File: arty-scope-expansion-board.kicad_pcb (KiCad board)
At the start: 4 copper layers, 109 x 86 mm, 75 parts, among them J1 PMOD_A, J2 PMOD_B, J3 PMOD_C, J4 PMOD_D, J5 Conn_Coaxial, U1 AD9288, U2 74LS374, U3 74LS374, U4 AD8370AREZ-RL7, U5 AD8132ARZ, U6 AD8132ARZ, U7 MCP4822

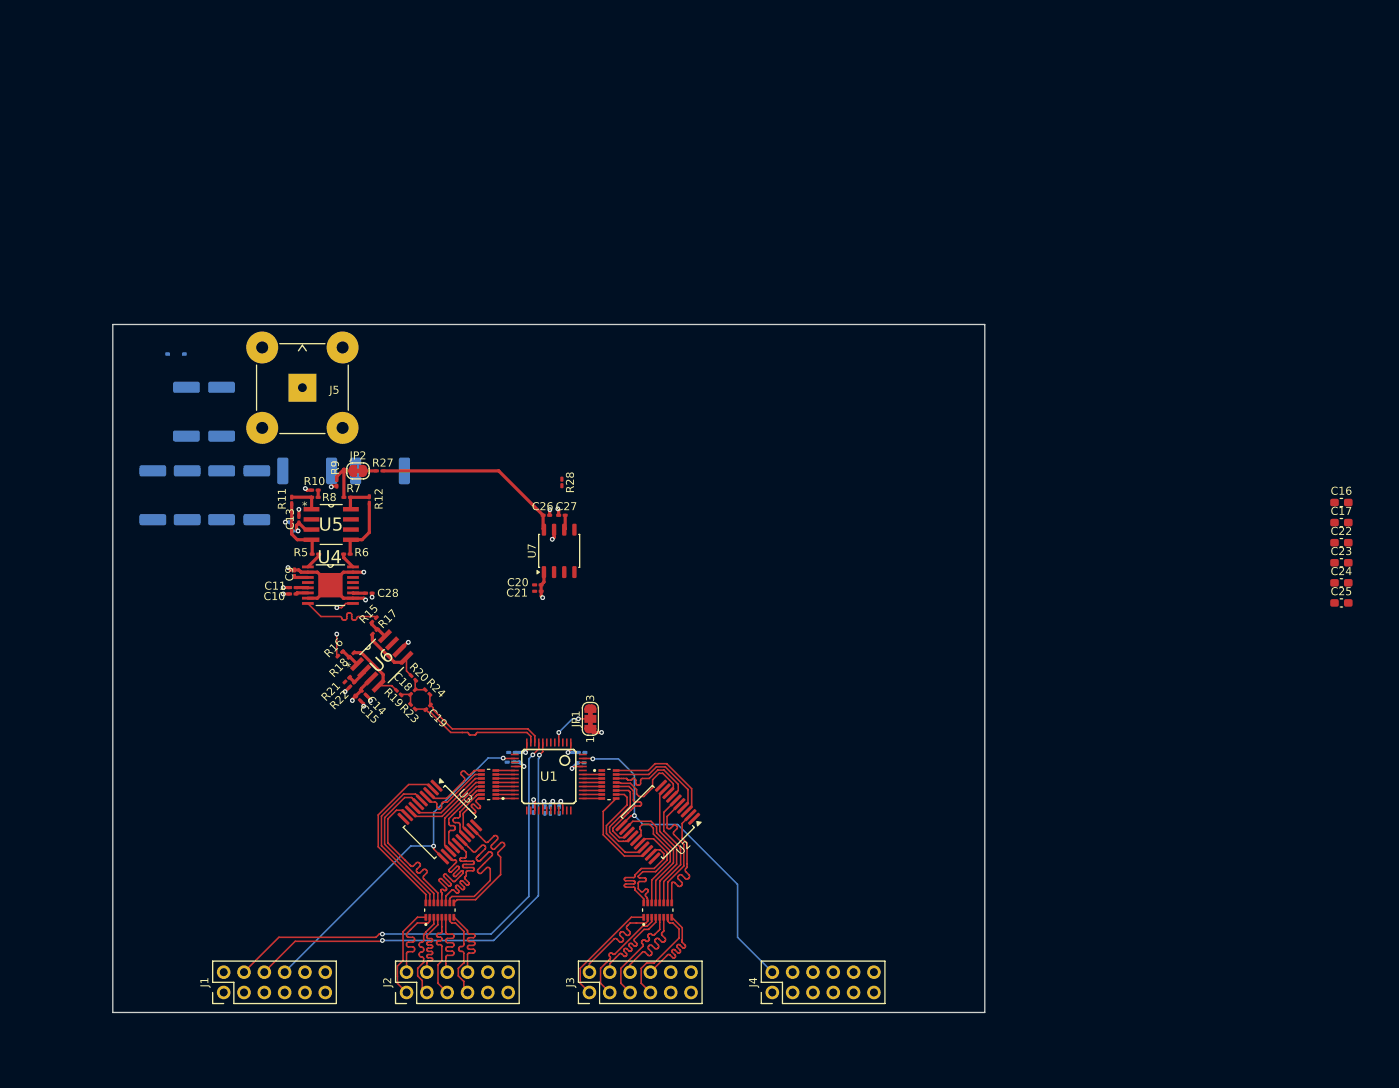
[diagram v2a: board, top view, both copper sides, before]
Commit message: [feat] Added power planes with LDO's and changed footprints to correct ones
Two power planes where added:
- 3.3V powered by Arty via LDO
- 5V powered via gpio via LDO (can be powered by Arty 5V - i think)
Changed smaller capacitors sizes to correct ones. In prevous iterations
i missmached metric footprints with imperial ones.
Rerouted whole input stage.
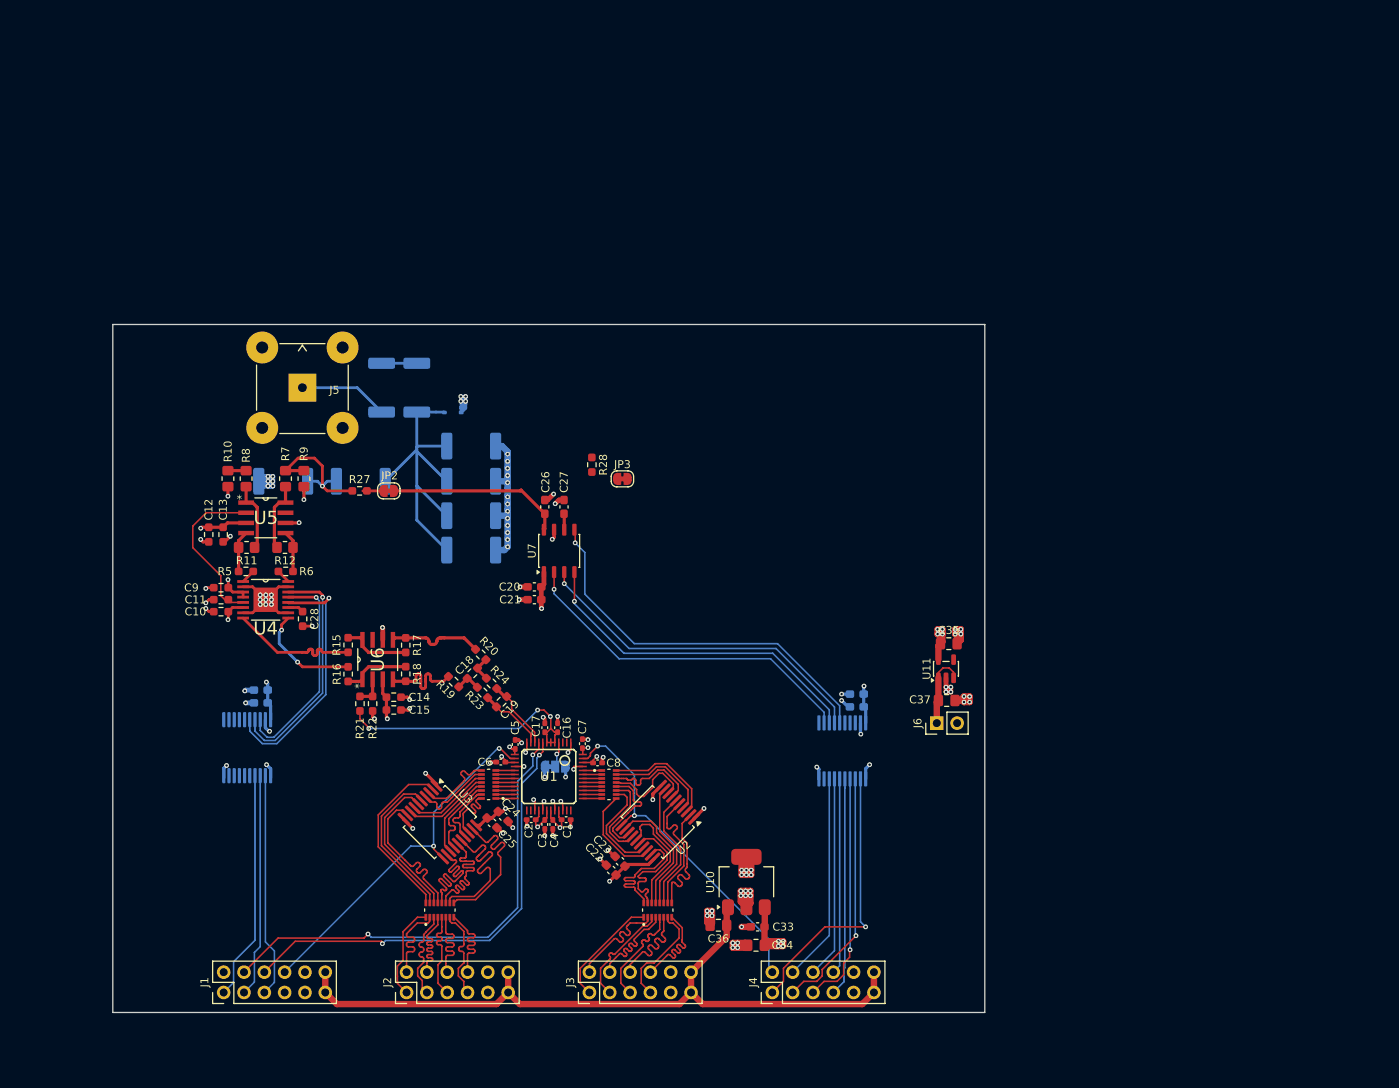
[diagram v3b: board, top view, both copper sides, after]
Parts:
- added C29: 100n, Capacitor_SMD:C_0603_1608Metric_Pad1.08x0.95mm_HandSolder, B.Cu at (134.0, 84.3)
- added C30: 10u, Capacitor_SMD:C_0603_1608Metric_Pad1.08x0.95mm_HandSolder, B.Cu at (134.0, 82.7)
- added C31: 100n, Capacitor_SMD:C_0603_1608Metric_Pad1.08x0.95mm_HandSolder, B.Cu at (208.5, 84.8)
- added C32: 10u, Capacitor_SMD:C_0603_1608Metric_Pad1.08x0.95mm_HandSolder, B.Cu at (208.5, 83.2)
- added C33: 100n, Capacitor_SMD:C_0603_1608Metric_Pad1.08x0.95mm_HandSolder, F.Cu at (196.1, 112.3)
- added C34: 1u, Capacitor_SMD:C_0805_2012Metric_Pad1.18x1.45mm_HandSolder, F.Cu at (195.9, 114.6)
- added C35: 1u, Capacitor_SMD:C_0805_2012Metric_Pad1.18x1.45mm_HandSolder, F.Cu at (220.0, 76.9)
- added C36: 4u7, Capacitor_SMD:C_0805_2012Metric_Pad1.18x1.45mm_HandSolder, F.Cu at (191.2, 112.1)
- added C37: 1u, Capacitor_SMD:C_0805_2012Metric_Pad1.18x1.45mm_HandSolder, F.Cu at (219.7, 84.0)
- added J6: Conn_01x02_Pin, Connector_PinHeader_2.54mm:PinHeader_1x02_P2.54mm_Vertical, F.Cu at (218.5, 86.8)
- added JP3: Jumper_2_Bridged, Jumper:SolderJumper-2_P1.3mm_Bridged_RoundedPad1.0x1.5mm, F.Cu at (179.2, 56.3)
- added U10: MCP1826S, Package_TO_SOT_SMD:SOT-223-3_TabPin2, F.Cu at (194.7, 106.7)
- added U11: MIC5504-3.3YM5, Package_TO_SOT_SMD:SOT-23-5, F.Cu at (219.7, 80.0)
- added U8: 74AHCT541, Package_SO:SSOP-20_5.3x7.2mm_P0.65mm, B.Cu at (132.3, 89.9)
- added U9: 74AHCT541, Package_SO:SSOP-20_5.3x7.2mm_P0.65mm, B.Cu at (206.7, 90.3)
- C1, C2, C3, C4, C5, C6, C7, C8: footprint Capacitor_SMD:C_0201_0603Metric_Pad0.64x0.40mm_HandSolder -> Capacitor_SMD:C_0402_1005Metric_Pad0.74x0.62mm_HandSolder; moved to F.Cu
- C10, C11, C13, C14, C15, C18, C19, C28, C9: footprint Capacitor_SMD:C_0201_0603Metric_Pad0.64x0.40mm_HandSolder -> Resistor_SMD:R_0603_1608Metric_Pad0.98x0.95mm_HandSolder
- C12: footprint Capacitor_SMD:C_0201_0603Metric_Pad0.64x0.40mm_HandSolder -> Resistor_SMD:R_0603_1608Metric_Pad0.98x0.95mm_HandSolder; moved to F.Cu
- C16, C17: footprint Capacitor_SMD:C_0603_1608Metric_Pad1.08x0.95mm_HandSolder -> Capacitor_SMD:C_0402_1005Metric_Pad0.74x0.62mm_HandSolder
- C20, C21, C26, C27: footprint Capacitor_SMD:C_0201_0603Metric_Pad0.64x0.40mm_HandSolder -> Capacitor_SMD:C_0603_1608Metric_Pad1.08x0.95mm_HandSolder
- D3: value SD24C-01F -> CDSOD323-T24C
- JP1: footprint Jumper:SolderJumper-3_P1.3mm_Bridged123_RoundedPad1.0x1.5mm_NumberLabels -> Jumper:SolderJumper-3_P1.3mm_Bridged12_RoundedPad1.0x1.5mm_NumberLabels; moved to B.Cu
- R10, R11, R12, R7, R8, R9: footprint Resistor_SMD:R_0201_0603Metric_Pad0.64x0.40mm_HandSolder -> Resistor_SMD:R_0805_2012Metric_Pad1.20x1.40mm_HandSolder
- R15, R16, R17, R18, R19, R20, R21, R22, R23, R24, R27, R28, R5, R6: footprint Resistor_SMD:R_0201_0603Metric_Pad0.64x0.40mm_HandSolder -> Resistor_SMD:R_0603_1608Metric_Pad0.98x0.95mm_HandSolder
- moved C25 109.7 mm to (162.9, 99.3), turned to -45 degrees
- moved C24 108.8 mm to (164.3, 98.5), turned to -45 degrees
- moved C17 102.8 mm to (169.5, 87.4), turned to -90 degrees
- moved C16 101.9 mm to (171.1, 87.4), turned to -90 degrees
- moved C22 100.0 mm to (177.8, 105.2), turned to 135 degrees
- moved C23 97.6 mm to (178.9, 104.1), turned to 135 degrees
- moved R14 40.4 mm to (160.3, 65.2), turned to 0 degrees
- moved R25 35.6 mm to (160.3, 60.9), turned to 0 degrees
- moved D3 35.4 mm to (158.0, 48.0), turned to 0 degrees
- moved R26 31.2 mm to (160.3, 56.6), turned to 0 degrees
- moved R13 29.0 mm to (153.5, 44.9), turned to 90 degrees
- moved R2 27.5 mm to (160.3, 52.2), turned to 0 degrees
- moved R1 20.2 mm to (149.1, 44.9), turned to -90 degrees
- moved R4 12.2 mm to (136.8, 56.6), turned to 180 degrees
- moved R12 12.1 mm to (137.0, 64.9), turned to 180 degrees
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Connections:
- C26 pad 1: Net-(U7-VA) -> Net-(JP2-A)
- C27 pad 1: Net-(U7-VB) -> Net-(JP3-A)
- J1 pad 1: PGA_CLK_A -> PGA_LATCH_A_3.3V
- J1 pad 11: +3.3VCC -> VIN_3.3V
- J1 pad 12: +3.3VCC -> VIN_3.3V
- J1 pad 3: PGA_DATA_A -> PGA_DATA_A_3.3V
- J1 pad 5: PGA_LATCH_A -> PGA_CLK_A_3.3V
- J2 pad 11: +3.3VCC -> VIN_3.3V
- J2 pad 12: +3.3VCC -> VIN_3.3V
- J3 pad 11: +3.3VCC -> VIN_3.3V
- J3 pad 12: +3.3VCC -> VIN_3.3V
- J4 pad 1: PGA_CLK_B -> PGA_CLK_B_3.3V
- J4 pad 11: +3.3VCC -> VIN_3.3V
- J4 pad 12: +3.3VCC -> VIN_3.3V
- J4 pad 3: PGA_DATA_B -> PGA_DATA_B_3.3V
- J4 pad 4: DAC_CS -> DAC_CS_3.3V
- J4 pad 5: PGA_LATCH_B -> PGA_LATCH_B_3.3V
- J4 pad 6: DAC_SDI -> DAC_SDI_3.3V
- J4 pad 7: DAC_LDAC -> DAC_LDAC_3.3V
- J4 pad 8: DAC_SCK -> DAC_SCK_3.3V
- JP1 pad 3: VDD -> +3.3VCC
- JP2 pad 1: DAC_A -> Net-(JP2-A)
- JP2 pad 2: SIG_A -> Net-(JP2-B)
- R27 pad 2: Net-(U7-VA) -> Net-(JP2-B)
- R28 pad 2: Net-(U7-VB) -> Net-(JP3-B)
- R3 pad 1: SIG_A -> DAC_A
- R4 pad 1: SIG_A -> DAC_A
- R7 pad 1: SIG_A -> DAC_A
- R9 pad 2: SIG_A -> DAC_A
- U4 pad 12: PGA_LATCH_A -> PGA_LATCH_A_5V
- U4 pad 13: PGA_CLK_A -> PGA_CLK_A_5V
- U4 pad 14: PGA_DATA_A -> PGA_DATA_A_5V
- U7 pad 2: DAC_CS -> DAC_CS_5V
- U7 pad 3: DAC_SCK -> DAC_SCK_5V
- U7 pad 4: DAC_SDI -> DAC_SDI_5V
- U7 pad 5: DAC_LDAC -> DAC_LDAC_5V
- U7 pad 6: Net-(U7-VB) -> Net-(JP3-A)
- U7 pad 8: Net-(U7-VA) -> Net-(JP2-A)
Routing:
- net GND: track 52.8 -> 165.9 mm, vias 26 -> 120
- net VIN_3.3V: track 0.00 -> 92.4 mm
- net DAC_LDAC_5V: track 0.00 -> 48.4 mm, vias 0 -> 1
- net DAC_SCK_5V: track 0.00 -> 44.5 mm, vias 0 -> 1
- net DAC_CS_5V: track 0.00 -> 43.9 mm, vias 0 -> 1
- net DAC_SDI_5V: track 0.00 -> 42.9 mm, vias 0 -> 1
- net Net-(D3-A1): track 0.00 -> 42.3 mm
- net +3.3VCC: track 0.00 -> 40.3 mm, vias 0 -> 13
- net PGA_CLK_B_3.3V: track 0.00 -> 34.8 mm, vias 0 -> 1
- net REFOUT: track 0.00 -> 34.0 mm, vias 0 -> 3
- net PGA_LATCH_A_5V: track 0.00 -> 31.4 mm, vias 0 -> 1
- net PGA_DATA_B_3.3V: track 0.00 -> 31.0 mm, vias 0 -> 1
- net PGA_LATCH_B_3.3V: track 0.00 -> 29.6 mm, vias 0 -> 1
- net PGA_DATA_A_5V: track 0.00 -> 29.2 mm, vias 0 -> 1
- net PGA_LATCH_A_3.3V: track 0.00 -> 28.4 mm
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- added copper zone on In2.Cu, net +3.3VCC
- added copper zone on In2.Cu, net +5VCC

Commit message: [feat] Added second channel with routing
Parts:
- added C38: 100n, Resistor_SMD:R_0603_1608Metric_Pad0.98x0.95mm_HandSolder, F.Cu at (199.7, 69.9)
- added C39: 1n, Resistor_SMD:R_0603_1608Metric_Pad0.98x0.95mm_HandSolder, F.Cu at (199.7, 72.9)
- added C40: 1n, Resistor_SMD:R_0603_1608Metric_Pad0.98x0.95mm_HandSolder, F.Cu at (209.9, 73.8)
- added C41: 100n, Resistor_SMD:R_0603_1608Metric_Pad0.98x0.95mm_HandSolder, F.Cu at (189.3, 74.1)
- added C42: 10u, Resistor_SMD:R_0603_1608Metric_Pad0.98x0.95mm_HandSolder, F.Cu at (189.3, 72.5)
- added C43: 47p, Resistor_SMD:R_0603_1608Metric_Pad0.98x0.95mm_HandSolder, F.Cu at (179.5, 80.5)
- added C44: 1n, Resistor_SMD:R_0603_1608Metric_Pad0.98x0.95mm_HandSolder, F.Cu at (199.5, 71.4)
- added C45: 10p, Resistor_SMD:R_0603_1608Metric_Pad0.98x0.95mm_HandSolder, F.Cu at (175.9, 84.2)
- added C46: 100n, Resistor_SMD:R_0603_1608Metric_Pad0.98x0.95mm_HandSolder, F.Cu at (200.0, 63.2)
- added C47: 10u, Resistor_SMD:R_0603_1608Metric_Pad0.98x0.95mm_HandSolder, F.Cu at (198.2, 63.2)
- added D4: CDSOD323-T24C, Diode_SMD:D_SOD-323, B.Cu at (182.0, 48.0)
- added J7: Conn_Coaxial, Connector_Coaxial:BNC_TEConnectivity_1478035_Horizontal, F.Cu at (200.8, 44.9)
- added R29: 499, Resistor_SMD:R_0603_1608Metric_Pad0.98x0.95mm_HandSolder, F.Cu at (195.0, 80.7)
- added R30: 499, Resistor_SMD:R_0603_1608Metric_Pad0.98x0.95mm_HandSolder, F.Cu at (195.0, 77.0)
- added R31: 11, Resistor_SMD:R_2512_6332Metric_Pad1.40x3.35mm_HandSolder, B.Cu at (190.9, 44.9)
- added R32: 499, Resistor_SMD:R_0603_1608Metric_Pad0.98x0.95mm_HandSolder, F.Cu at (187.8, 80.6)
- added R33: 499, Resistor_SMD:R_0603_1608Metric_Pad0.98x0.95mm_HandSolder, F.Cu at (187.8, 77.0)
- added R34: 11, Resistor_SMD:R_2512_6332Metric_Pad1.40x3.35mm_HandSolder, B.Cu at (186.4, 45.0)
- added R35: 222, Resistor_SMD:R_2512_6332Metric_Pad1.40x3.35mm_HandSolder, B.Cu at (179.7, 52.2)
- added R36: 222, Resistor_SMD:R_2512_6332Metric_Pad1.40x3.35mm_HandSolder, B.Cu at (179.7, 56.6)
- added R37: 222, Resistor_SMD:R_2512_6332Metric_Pad1.40x3.35mm_HandSolder, B.Cu at (179.7, 60.9)
- added R38: 222, Resistor_SMD:R_2512_6332Metric_Pad1.40x3.35mm_HandSolder, B.Cu at (179.7, 65.2)
- added R39: 499, Resistor_SMD:R_2512_6332Metric_Pad1.40x3.35mm_HandSolder, B.Cu at (193.5, 56.6)
- added R40: 55.6, Resistor_SMD:R_2512_6332Metric_Pad1.40x3.35mm_HandSolder, B.Cu at (203.2, 56.6)
- added R41: 100, Resistor_SMD:R_0603_1608Metric_Pad0.98x0.95mm_HandSolder, F.Cu at (181.9, 81.6)
- added R42: 100, Resistor_SMD:R_0603_1608Metric_Pad0.98x0.95mm_HandSolder, F.Cu at (178.5, 78.2)
- added R43: 49.9, Resistor_SMD:R_0603_1608Metric_Pad0.98x0.95mm_HandSolder, F.Cu at (178.2, 83.0)
- added R44: 49.9, Resistor_SMD:R_0603_1608Metric_Pad0.98x0.95mm_HandSolder, F.Cu at (177.1, 81.8)
- added R45: 2.61k, Resistor_SMD:R_0603_1608Metric_Pad0.98x0.95mm_HandSolder, F.Cu at (193.6, 73.3)
- added R46: 10k, Resistor_SMD:R_0603_1608Metric_Pad0.98x0.95mm_HandSolder, F.Cu at (192.0, 73.3)
- added R47: 55.6, Resistor_SMD:R_0805_2012Metric_Pad1.20x1.40mm_HandSolder, F.Cu at (210.1, 56.2)
- added R48: 27.8, Resistor_SMD:R_0805_2012Metric_Pad1.20x1.40mm_HandSolder, F.Cu at (200.6, 56.2)
- added R49: 499, Resistor_SMD:R_0805_2012Metric_Pad1.20x1.40mm_HandSolder, F.Cu at (207.8, 56.2)
- added R50: 499, Resistor_SMD:R_0805_2012Metric_Pad1.20x1.40mm_HandSolder, F.Cu at (202.9, 56.2)
- added R51: 499, Resistor_SMD:R_0805_2012Metric_Pad1.20x1.40mm_HandSolder, F.Cu at (207.7, 64.8)
- added R52: 499, Resistor_SMD:R_0805_2012Metric_Pad1.20x1.40mm_HandSolder, F.Cu at (202.9, 64.8)
- added R53: 100, Resistor_SMD:R_0603_1608Metric_Pad0.98x0.95mm_HandSolder, F.Cu at (202.9, 67.8)
- added R54: 100, Resistor_SMD:R_0603_1608Metric_Pad0.98x0.95mm_HandSolder, F.Cu at (207.8, 67.8)
- added U12: AD8132ARZ, inzynierka.Library:SOIC127P600X175-8N, F.Cu at (191.3, 78.8)
- added U13: AD8370AREZ-RL7, inzynierka.Library:SOP65P640X120-17N, F.Cu at (205.3, 71.4)
- added U14: AD8132ARZ, inzynierka.Library:SOIC127P600X175-8N, F.Cu at (205.3, 61.1)
- moved R28 20.2 mm to (195.4, 57.2), turned to 180 degrees
- moved JP3 12.8 mm to (191.9, 57.2)
- moved C31 1.98 mm to (210.5, 84.7), turned to 180 degrees
- moved C32 1.97 mm to (210.5, 83.2), turned to 180 degrees
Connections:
- U1 pad 2: unconnected-(U1-AINA-Pad2) -> AINB+
- U1 pad 3: unconnected-(U1-/AINA-Pad3) -> AINB-
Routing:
- net GND: track 165.9 -> 233.7 mm, vias 120 -> 165
- net Net-(D4-A1): track 0.00 -> 42.3 mm
- net Net-(JP3-A): track 2.00 -> 24.2 mm
- net PGA_CLK_B_5V: track 0.00 -> 21.8 mm, vias 0 -> 1
- net PGA_DATA_B_5V: track 0.00 -> 21.6 mm, vias 0 -> 1
- net VOCM_B: track 0.00 -> 21.1 mm
- net DAC_B: track 0.00 -> 21.0 mm, vias 0 -> 1
- net PGA_LATCH_B_5V: track 0.00 -> 19.6 mm, vias 0 -> 1
- net +5VCC: track 40.0 -> 57.9 mm, vias 11 -> 15
- net OP_B-: track 0.00 -> 16.5 mm
- net OP_B+: track 0.00 -> 13.3 mm, vias 0 -> 2
- net Net-(U12--OUT): track 0.00 -> 12.6 mm
- net Net-(J7-In): track 0.00 -> 11.2 mm
- net Net-(U12-+OUT): track 0.00 -> 9.47 mm, vias 0 -> 2
- net AINB-: track 0.00 -> 8.83 mm
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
